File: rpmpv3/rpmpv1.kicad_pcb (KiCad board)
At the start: 2 copper layers, 96.1 x 64.4 mm, 31 parts, among them J1 RPi_GPIO, J2 Conn_01x07, P1 CONN_02X25, U1 MaxII_EPM240, U2 74LS245, U3 74LS245, U4 74LS245, U5 74LS245, U6 74LS05

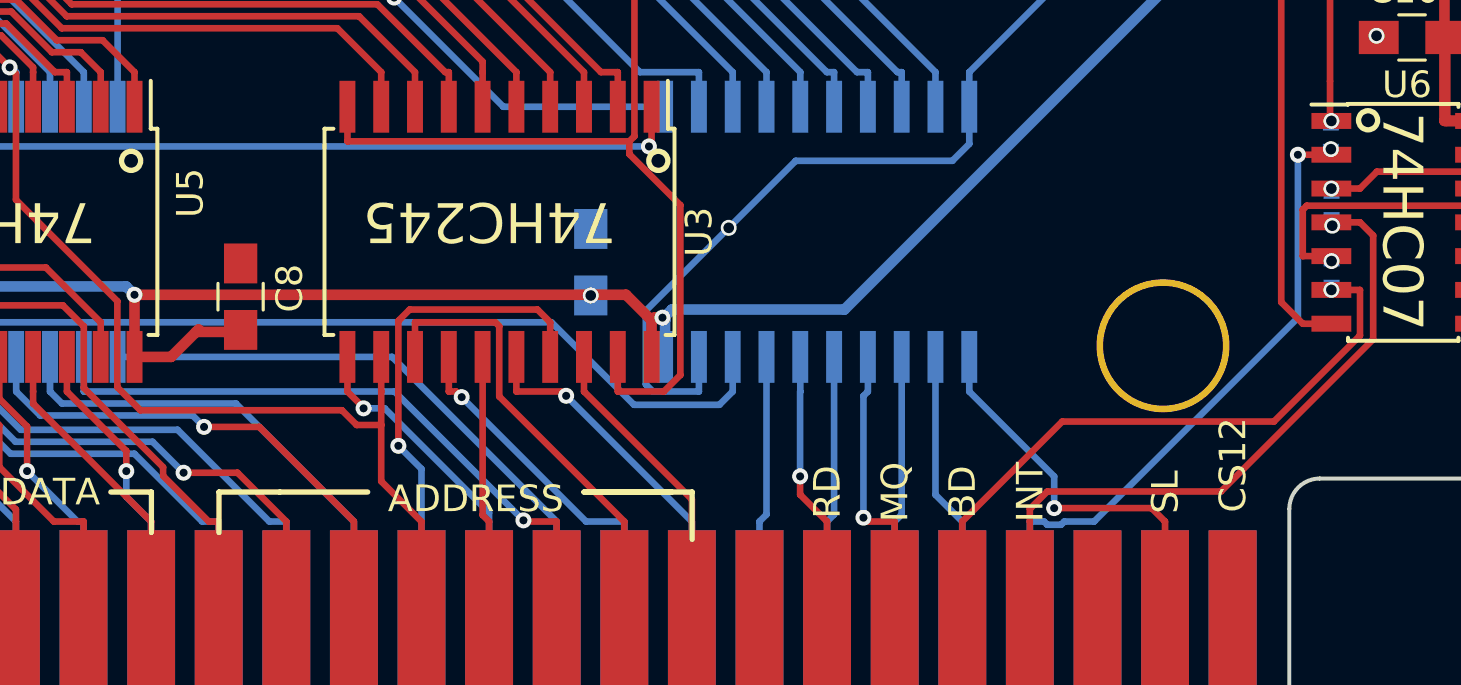
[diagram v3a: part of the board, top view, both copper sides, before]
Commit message: revised rpmpv3, rpmpv4
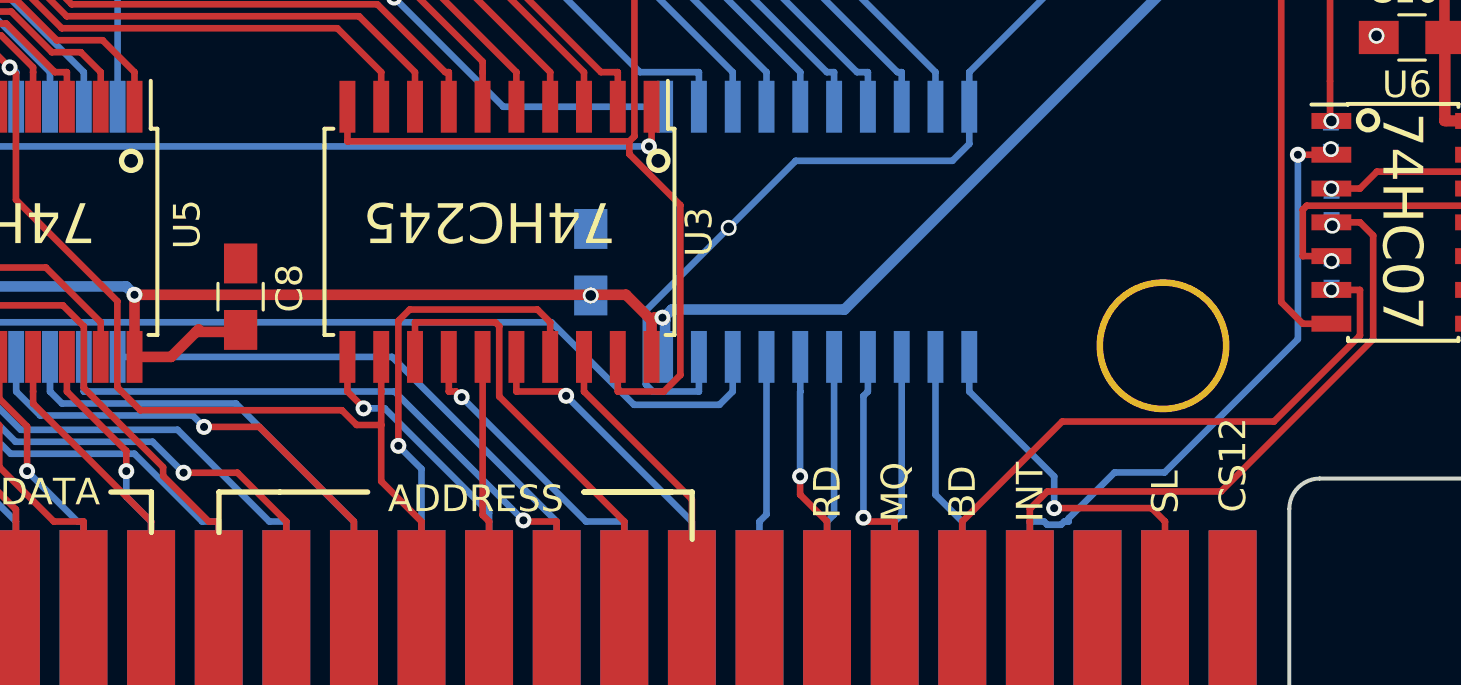
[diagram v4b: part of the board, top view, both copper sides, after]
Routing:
- net /WAIT: track 25.3 -> 25.8 mm
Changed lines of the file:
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@@
     (links 194)
     (no_connects 0)
-    (area 98.0821 49.444611 204.086546 115.286853)
+    (area 105.715999 49.581999 202.005001 114.133701)
     (thickness 1.6)
     (drawings 79)
-    (tracks 1127)
+    (tracks 1131)
     (zones 0)
     (modules 31)
@@
     (tags "SOIC 1.27")
     (attr smd)
-    (fp_text reference U5 (at -1.4615 -7.8105 270) (layer F.SilkS)
+    (fp_text reference U5 (at -0.2804 -7.6962 270) (layer F.SilkS)
       (effects (font (size 1 1) (thickness 0.15)))
     )
@@
   (segment (start 158.5907 76.327) (end 158.5907 75.9597) (width 0.25) (layer F.Cu) (net 10))
   (segment (start 159.766 76.327) (end 158.5907 76.327) (width 0.25) (layer F.Cu) (net 10))
+  (segment (start 181.7878 105.5021) (end 181.7878 105.3846) (width 0.25) (layer B.Cu) (net 11))
+  (segment (start 190.4019 98.6501) (end 190.4019 97.8461) (width 0.25) (layer B.Cu) (net 11))
+  (segment (start 185.3946 103.6574) (end 190.4019 98.6501) (width 0.25) (layer B.Cu) (net 11))
+  (segment (start 183.515 103.6574) (end 185.3946 103.6574) (width 0.25) (layer B.Cu) (net 11))
+  (segment (start 181.7878 105.3846) (end 183.515 103.6574) (width 0.25) (layer B.Cu) (net 11))
   (via (at 191.643 91.509) (size 0.6) (drill 0.4) (layers F.Cu B.Cu) (net 11))
   (segment (start 191.643 91.509) (end 191.661 91.527) (width 0.25) (layer F.Cu) (net 11))
   (segment (start 191.661 91.527) (end 191.661 91.7194) (width 0.25) (layer F.Cu) (net 11))
   (via (at 190.4019 91.7194) (size 0.6) (layers F.Cu B.Cu) (net 11))
+  (segment (start 190.4019 97.8461) (end 190.4019 91.7194) (width 0.25) (layer B.Cu) (net 11))
   (segment (start 191.661 91.7194) (end 190.4019 91.7194) (width 0.25) (layer F.Cu) (net 11))
-  (segment (start 190.4019 97.8461) (end 190.4019 91.7194) (width 0.25) (layer B.Cu) (net 11))
   (segment (start 180.3298 109.8274) (end 180.3298 105.5021) (width 0.25) (layer B.Cu) (net 11))
   (segment (start 180.9853 105.6237) (end 181.5034 105.6237) (width 0.25) (layer B.Cu) (net 11))
@@
   (segment (start 180.3298 105.5021) (end 180.8637 105.5021) (width 0.25) (layer B.Cu) (net 11))
   (segment (start 181.5034 105.6237) (end 181.625 105.5021) (width 0.25) (layer B.Cu) (net 11))
-  (segment (start 182.7459 105.5021) (end 190.4019 97.8461) (width 0.25) (layer B.Cu) (net 11))
-  (segment (start 181.625 105.5021) (end 182.7459 105.5021) (width 0.25) (layer B.Cu) (net 11))
+  (segment (start 181.625 105.5021) (end 181.7878 105.5021) (width 0.25) (layer B.Cu) (net 11))
   (segment (start 191.6684 94.0744) (end 191.6684 94.361) (width 0.25) (layer B.Cu) (net 12))
   (segment (start 191.6938 94.3864) (end 191.661 94.3536) (width 0.25) (layer F.Cu) (net 12))
